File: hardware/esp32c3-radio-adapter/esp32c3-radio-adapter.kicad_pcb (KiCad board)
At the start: 2 copper layers, 29 x 36.5 mm, 10 parts, among them J1 Conn_01x08, J2 Conn_01x08, J3 E07-M1101D_or_Ra-02, J4 Expansion

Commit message: Adapters: GPIO map that lets the same socket take all three radio boards
The green D-Sun CC1101 board plugs into the socket adapter's 2x4 socket
too; only its signal order differs, which the firmware absorbs with a pin
map per board.  What the hardware must guarantee is that no socket
position that carries a radio OUTPUT on any of the boards is an ESP32-C3
boot strapping pin (GPIO2/8/9).  Only position 4 (blue CSN, green SCK,
Ra-02 NSS) is an input on every board, so it takes GPIO9; GPIO8 moves to
the spare header and positions 5 and 6 are fed from GPIO3 and GPIO4.

Socket positions 3..8 are now GPIO10, 9, 3, 4, 7, 6.  Per-board maps:
blue E07 MOSI 4 SCK 3 CSN 9 MISO 7 GDO0 10 GDO2 6; green D-Sun MOSI 10
SCK 9 CSN 6 MISO 3 GDO0 7 GDO2 4; Ra-02 MOSI 4 SCK 3 NSS 9 MISO 7 RST 10
DIO0 6.  The README also describes telling the two CC1101 boards apart
passively at power-up (an unconfigured CC1101 clocks XOSC/192 out of
GDO0, on GPIO10 for the blue board and GPIO7 for the green).

Socket adapter routing, still entirely on the back copper: GPIO9 leaves
its pad sideways into the gap before GPIO10 and drops into position 4;
MISO takes the column under GPIO8's pad; SCK and MOSI come down from the
power row through the gaps either side of GPIO8's pad, and GPIO8 climbs
between them to the header (now 3V3, 8, 2, 1, 0, 21TX, 20RX).

SX1278 module adapter: same GPIOs with MOSI and SCK swapped (GPIO3/4) so
its bottom copper nests, NSS on GPIO9 via the top-copper bus, RESET on
GPIO8 (an ESP32 output).

Jumper-wire diagrams: one layout serves all three boards; GPIO4 and GPIO3
take the ribbon's white and black; the Ra-02 strap goes to GPIO1 (GPIO4
is now MOSI).  Both adapters pass ERC and DRC.

Co-Authored-By: Claude Fable 5.1 <noreply@anthropic.com>
Claude-Session: https://claude.ai/code/session_01JoGdh4Cg3VtTTDZi4gQuiN
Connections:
- J1 pad 4: MOSI -> GPIO8
- J1 pad 5: SCK -> CSN_NSS
- J2 pad 4: GPIO4 -> MOSI
- J2 pad 5: GPIO3 -> SCK
- J2 pad 8: CSN_NSS -> GPIO0
- J4 pad 2: GPIO4 -> GPIO8
- J4 pad 3: GPIO3 -> GPIO2
- J4 pad 4: GPIO2 -> GPIO1
- J4 pad 5: GPIO1 -> GPIO0
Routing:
- net GPIO8: track 0.00 -> 21.7 mm
- net CSN_NSS: track 32.2 -> 11.8 mm
- net SCK: track 6.76 -> 24.5 mm
- net MOSI: track 11.8 -> 29.6 mm
- net GPIO0: track 0.00 -> 6.43 mm
- net GPIO4: track 5.01 -> 0.00 mm
- net GPIO3: track 5.01 -> 0.00 mm
- net GPIO2: track 5.01 -> 6.43 mm
- net GPIO1: track 5.01 -> 6.43 mm
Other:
- board text added: "E07-M1101D / D-Sun / Ra-02"
- board text removed: "E07-M1101D (Ra-02 breakout)"

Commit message: Socket adapter: move CSN/NSS off the GPIO9 boot strap to GPIO1
On the bench (2026-09-06) the CC1101/Ra-02 nodes powered straight into USB
download mode every reset and never ran the firmware.  Root cause: socket
position 4 (CSN on the blue board, SCK on the green, NSS on the Ra-02) was
GPIO9, the ESP32-C3 BOOT strap.  A radio pin loads that net with enough
capacitance that, through the chip's weak internal pull-up, it rises too
slowly for the mask ROM to read it high at reset, so the ROM latches BOOT low
and enters download mode.  It is not the firmware -- the ROM samples the strap
before any code runs -- and it is not fixable in software.

Fix, single layer as before: position 4 now takes GPIO1 (routed from the power
row, across between the SuperMini rows and into the pad from the left).  GPIO9
is left unconnected -- an unconnected strap floats high on the internal
pull-up, the safest state -- so the socket now carries no strap at all.  The
expansion header keeps its proven 7-pin geometry: GPIO1's old slot becomes a
second 3V3, and GPIO8/GPIO2 (the straps that stay exposed there) each get an
optional do-not-populate pull-up-to-3V3 footprint (R2/R3) bridging to the
adjacent 3V3 pin.  ERC/DRC clean.

Firmware pin map changes by one pin only: CSN/SCK/NSS 9 -> 1; everything else
unchanged.

Co-Authored-By: Claude Opus 4.8 <noreply@anthropic.com>
Claude-Session: https://claude.ai/code/session_01JoGdh4Cg3VtTTDZi4gQuiN
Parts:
- added R2: 4k7, Adapter:R_0805_HeaderPullup, F.Cu at (108.2, 102.5)
- added R3: 4k7, Adapter:R_0805_HeaderPullup, F.Cu at (113.2, 102.5)
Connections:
- J1 pad 5: CSN_NSS -> GPIO9
- J2 pad 7: GPIO1 -> CSN_NSS
- J4 pad 4: GPIO1 -> +3V3
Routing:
- net CSN_NSS: track 11.8 -> 29.6 mm
- net GPIO1: track 6.43 -> 0.00 mm
- net +3V3: track 64.0 -> 65.4 mm
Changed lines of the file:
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@@
 	(net 3 "MISO")
 	(net 4 "GPIO8")
-	(net 5 "CSN_NSS")
+	(net 5 "GPIO9")
 	(net 6 "GDO0_RST")
 	(net 7 "GPIO20")
@@
 	(net 13 "SCK")
 	(net 14 "GPIO2")
-	(net 15 "GPIO1")
+	(net 15 "CSN_NSS")
 	(net 16 "GPIO0")
 	(footprint "Adapter:SuperMini_Row_1x08_P2.54mm_THT_Castellated_Down"
@@
 			(layers "*.Cu" "*.Mask")
 			(remove_unused_layers no)
-			(net 5 "CSN_NSS")
+			(net 5 "GPIO9")
 			(pinfunction "Pin_5")
 			(pintype "passive")
@@
 			(layers "*.Cu" "*.Mask")
 			(remove_unused_layers no)
-			(net 15 "GPIO1")
+			(net 15 "CSN_NSS")
 			(pinfunction "Pin_7")
 			(pintype "passive")
@@
 			(layers "*.Cu" "*.Mask")
 			(remove_unused_layers no)
-			(net 5 "CSN_NSS")
+			(net 15 "CSN_NSS")
 			(pinfunction "Pin_4")
 			(pintype "passive")
@@
 			(layers "*.Cu" "*.Mask")
 			(remove_unused_layers no)
-			(net 15 "GPIO1")
+			(net 11 "+3V3")
 			(pinfunction "Pin_4")
 			(pintype "passive")
@@
 		)
 	)
+	(footprint "Adapter:R_0805_HeaderPullup"
+		(layer "F.Cu")
+		(at 108.15 102.55)
+		(descr "0805 resistor bridging two adjacent 2.54 mm header pins, on the back copper (optional strap pull-up)")
+		(tags "resistor 0805 pull-up header")
+		(sheetname "/")
+		(sheetfile "esp32c3-radio-adapter.kicad_sch")
+		(property "Reference" "R2"
+			(at 0 -1.8 0)
+			(layer "F.SilkS")
+			(hide yes)
+			(effects
+				(font
+					(size 0.8 0.8)
+					(thickness 0.12)
+				)
+			)
+		)
+		(property "Value" "4k7"
+			(at 0 1.8 0)
+			(layer "F.Fab")
+			(hide yes)
+			(effects
+				(font
+					(size 0.8 0.8)
+					(thickness 0.12)
+				)
+			)
+		)
+		(property "Datasheet" ""
+			(at 0 0 0)
+			(layer "F.Fab")
+			(hide yes)
+			(effects
+				(font
+					(size 1.27 1.27)
+					(thickness 0.1905)
+				)
+			)
+		)
+		(property "Description" ""
+			(at 0 0 0)
+			(layer "F.Fab")
+			(hide yes)
+			(effects
+				(font
+					(size 1.27 1.27)
+					(thickness 0.1905)
+				)
+			)
+		)
+		(attr smd)
+		(fp_text user "${REFERENCE}"
+			(at 0 -1.8 0)
+			(layer "F.Fab")
+			(effects
+				(font
+					(size 0.6 0.6)
+					(thickness 0.09)
+				)
+			)
+		)
+		(fp_rect
+			(start -0.65 -1)
+			(end 0.65 1)
+			(stroke
+				(width 0.1)
+				(type solid)
+			)
+			(fill no)
+			(layer "B.Fab")
+		)
+		(pad "1" smd rect
+			(at -1.27 0)
+			(size 1.4 1.2)
+			(layers "B.Cu" "B.Mask" "B.Paste")
+			(net 11 "+3V3")
+			(pinfunction "Pin_1")
+			(pintype "passive")
+		)
+		(pad "2" smd rect
+			(at 1.27 0)
+			(size 1.4 1.2)
+			(layers "B.Cu" "B.Mask" "B.Paste")
+			(net 4 "GPIO8")
+			(pinfunction "Pin_2")
+			(pintype "passive")
+		)
+		(embedded_fonts no)
+	)
+	(footprint "Adapter:R_0805_HeaderPullup"
+		(layer "F.Cu")
+		(at 113.23 102.55)
+		(descr "0805 resistor bridging two adjacent 2.54 mm header pins, on the back copper (optional strap pull-up)")
+		(tags "resistor 0805 pull-up header")
+		(sheetname "/")
+		(sheetfile "esp32c3-radio-adapter.kicad_sch")
+		(property "Reference" "R3"
+			(at 0 -1.8 0)
+			(layer "F.SilkS")
+			(hide yes)
+			(effects
+				(font
+					(size 0.8 0.8)
+					(thickness 0.12)
+				)
+			)
+		)
+		(property "Value" "4k7"
+			(at 0 1.8 0)
+			(layer "F.Fab")
+			(hide yes)
+			(effects
+				(font
+					(size 0.8 0.8)
+					(thickness 0.12)
+				)
+			)
+		)
+		(property "Datasheet" ""
+			(at 0 0 0)
+			(layer "F.Fab")
+			(hide yes)
+			(effects
+				(font
+					(size 1.27 1.27)
+					(thickness 0.1905)
+				)
+			)
+		)
+		(property "Description" ""
+			(at 0 0 0)
+			(layer "F.Fab")
+			(hide yes)
+			(effects
+				(font
+					(size 1.27 1.27)
+					(thickness 0.1905)
+				)
+			)
+		)
+		(attr smd)
+		(fp_text user "${REFERENCE}"
+			(at 0 -1.8 0)
+			(layer "F.Fab")
+			(effects
+				(font
+					(size 0.6 0.6)
+					(thickness 0.09)
+				)
+			)
+		)
+		(fp_rect
+			(start -0.65 -1)
+			(end 0.65 1)
+			(stroke
+				(width 0.1)
+				(type solid)
+			)
+			(fill no)
+			(layer "B.Fab")
+		)
+		(pad "1" smd rect
+			(at -1.27 0)
+			(size 1.4 1.2)
+			(layers "B.Cu" "B.Mask" "B.Paste")
+			(net 14 "GPIO2")
+			(pinfunction "Pin_1")
+			(pintype "passive")
+		)
+		(pad "2" smd rect
+			(at 1.27 0)
+			(size 1.4 1.2)
+			(layers "B.Cu" "B.Mask" "B.Paste")
+			(net 11 "+3V3")
+			(pinfunction "Pin_2")
+			(pintype "passive")
+		)
+		(embedded_fonts no)
+	)
 	(footprint "Adapter:MountingHole_2.2mm_M2"
 		(layer "F.Cu")
@@
 		)
 	)
-	(gr_text "CSN/NSS"
-		(at 111.4 118.94 90)
-		(layer "F.SilkS")
-		(effects
-			(font
-				(size 0.5 0.5)
-				(thickness 0.075)
-			)
-		)
-	)
-	(gr_text "CSN/NSS"
-		(at 111.4 118.94 270)
-		(layer "B.SilkS")
-		(effects
-			(font
-				(size 0.5 0.5)
-				(thickness 0.075)
-			)
-			(justify mirror)
-		)
-	)
 	(gr_text "2"
 		(at 113.94 103.9 0)
@@
 	(gr_text "20"
 		(at 116.48 125.34 0)
+		(layer "B.SilkS")
+		(effects
+			(font
+				(size 0.5 0.5)
+				(thickness 0.075)
+			)
+			(justify mirror)
+		)
+	)
+	(gr_text "CSN/NSS"
+		(at 116.48 110.3 90)
+		(layer "F.SilkS")
+		(effects
+			(font
+				(size 0.5 0.5)
+				(thickness 0.075)
+			)
+		)
+	)
+	(gr_text "CSN/NSS"
+		(at 116.48 110.3 270)
 		(layer "B.SilkS")
 		(effects
@@
 		)
 	)
-	(gr_text "1"
+	(gr_text "3V3"
 		(at 114.5 101.25 0)
 		(layer "F.SilkS")
@@
 		)
 	)
-	(gr_text "1"
+	(gr_text "3V3"
 		(at 114.5 101.25 0)
 		(layer "B.SilkS")
@@
 	)
 	(segment
-		(start 111.4 122.24)
-		(end 112.67 122.24)
-		(width 0.25)
-		(layer "B.Cu")
-		(net 5)
-	)
-	(segment
-		(start 112.67 122.24)
+		(start 116.48 107)
+		(end 116.48 112)
+		(width 0.25)
+		(layer "B.Cu")
+		(net 15)
+	)
+	(segment
+		(start 116.48 112)
+		(end 112.67 112)
+		(width 0.25)
+		(layer "B.Cu")
+		(net 15)
+	)
+	(segment
+		(start 112.67 112)
 		(end 112.67 131.54)
 		(width 0.25)
 		(layer "B.Cu")
-		(net 5)
+		(net 15)
 	)
 	(segment
@@
 		(width 0.25)
 		(layer "B.Cu")
-		(net 5)
+		(net 15)
 	)
 	(segment
@@
 	)
 	(segment
+		(start 114.5 101.2)
+		(end 114.5 102.55)
+		(width 0.25)
+		(layer "B.Cu")
+		(net 11)
+	)
+	(segment
 		(start 113.94 107)
 		(end 113.94 104)
@@
 	)
 	(segment
-		(start 116.48 107)
-		(end 116.48 104)
-		(width 0.25)
-		(layer "B.Cu")
-		(net 15)
-	)
-	(segment
-		(start 116.48 104)
-		(end 114.5 104)
-		(width 0.25)
-		(layer "B.Cu")
-		(net 15)
-	)
-	(segment
-		(start 114.5 104)
-		(end 114.5 102.55)
-		(width 0.25)
-		(layer "B.Cu")
-		(net 15)
-	)
-	(segment

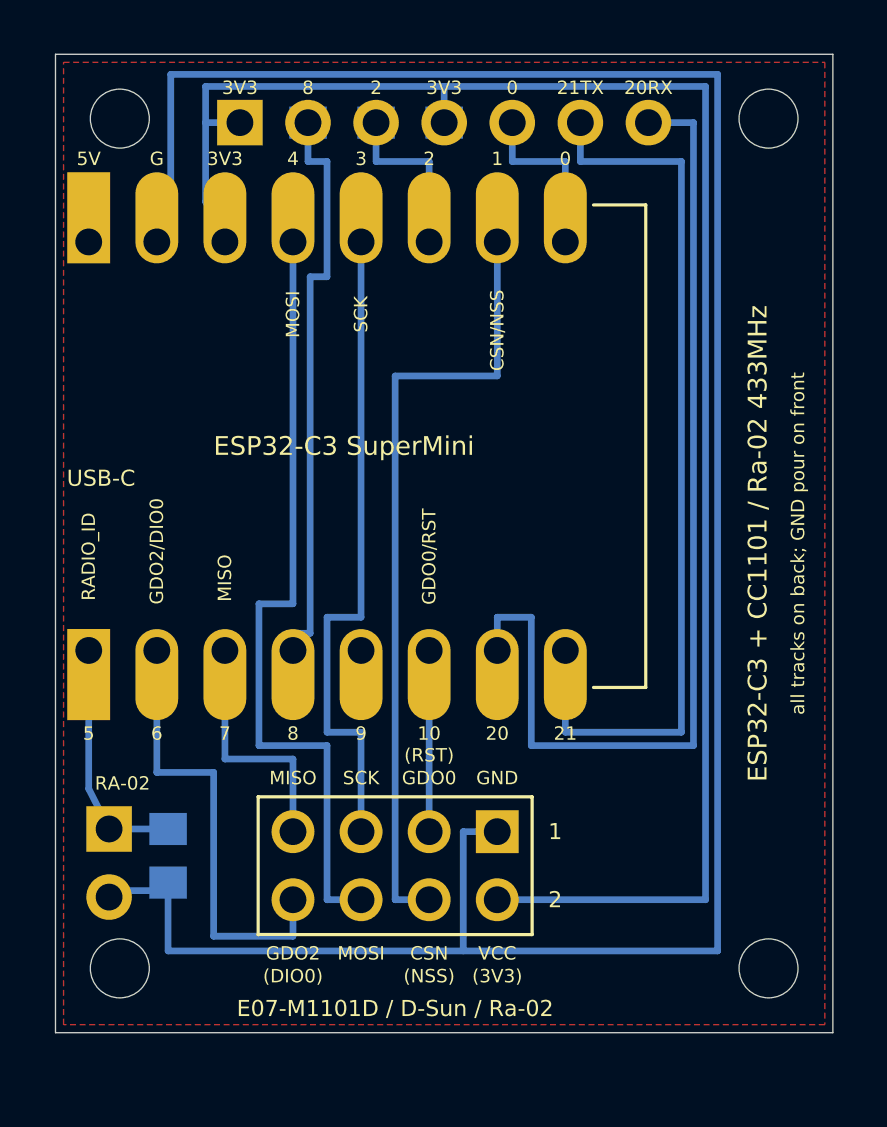
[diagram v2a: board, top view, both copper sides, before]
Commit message: Socket adapter: J5, a fly-wire header for the SX1278's DIO2/DATA pin
In the SX1278's continuous mode the raw bitstream reaches the outside
world only on DIO2/DATA -- the FIFO and packet handler are inactive, and
Table 29 gives no other DIO that can carry it in Rx.  Packet mode can't
stand in: it only carries what the chip's packet handler can frame, which
is fine for the Fineoffset stations but useless for the OOK remotes this
node exists to hear and key.  DIO2 is the SX1278's GDO2, and the Ra-02
breakout leaves it on the module edge, unconnected.

Add J5, a 1x2 header carrying GPIO21 and GPIO20, so one wire from an
Ra-02's DIO2 pad reaches a GPIO.  GPIO20 is that pin; both stay on J4 as
well, so nothing is lost -- one net, brought out twice.

Placing it took the board from 36.5 to 38.0 mm tall.  A 2.54 mm header
body and both plugged-in boards all sit at board level, so the header has
to be clear of them in plan view, and the only such region is the band
between the SuperMini's body and the radio board's top edge.  At 36.5 mm
that band is 4.08 mm, which leaves 0.79 mm either side of the body;
1.5 mm more opens it to 5.58 mm and takes both margins to 1.54 mm.

Routing stays single-sided.  GPIO21 drops right of GPIO20, so it must
take the lane above J5's pads (25.29) and stubs down into pin 1; GPIO20
takes the lane below (27.8) and climbs the strip straight through its own
pad, pin 2.  That fixes which net is on which pin: GPIO20's strip lane
has to pass through a pad of its own net, and the gap right of pin 2 is
only 0.235 mm.  The four strip lanes shift left 0.45 mm to make room
(GPIO21 22.9, GPIO20 23.35) and 3V3/GND move out to 24.55/25.0, still
0.375 mm clear of the M2 holes.

GND is not on J5: reaching it would mean crossing the 3V3 strip lane, and
it isn't needed -- the boards already share GND through the socket.

The SX1278 module adapter is untouched; its pin allocation is to be
brought into line with this board separately.

Co-Authored-By: Claude Opus 5 (1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
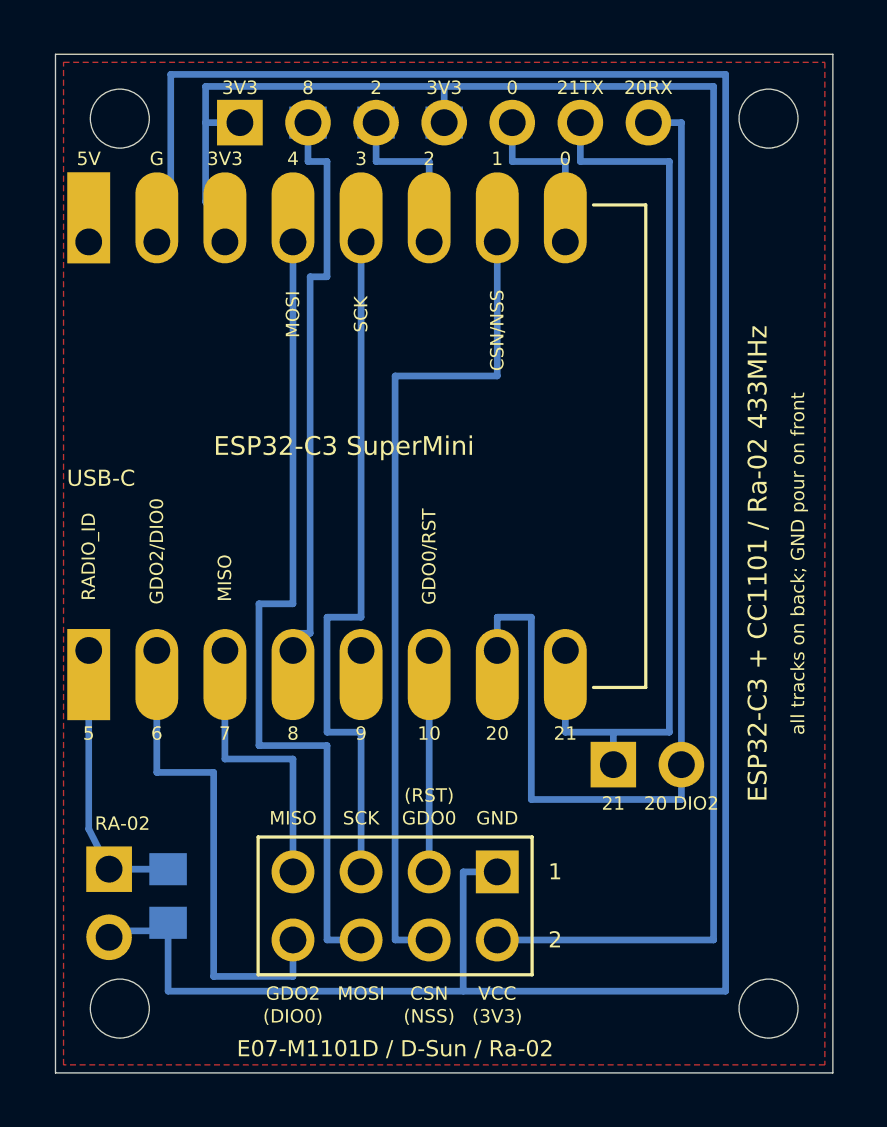
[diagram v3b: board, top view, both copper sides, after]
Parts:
- added J5: DIO2/DATA, Adapter:PinHeader_1x02_P2.54mm_Vertical, F.Cu at (120.8, 126.5)
- moved H3 1.50 mm to (102.4, 135.6)
- moved H4 1.50 mm to (126.6, 135.6)
- moved J3 1.50 mm to (116.5, 130.5)
- moved JP1 1.50 mm to (102.0, 130.4)
- moved R1 1.50 mm to (104.2, 131.4)
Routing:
- net GPIO20: track 38.3 -> 41.4 mm
- net GND: track 90.4 -> 92.5 mm
- net +3V3: track 65.4 -> 67.5 mm
- net SCK: track 24.5 -> 26.0 mm
- net RADIO_ID: track 9.04 -> 10.5 mm
- net MOSI: track 29.6 -> 31.1 mm
- net MISO: track 9.30 -> 10.8 mm
- net GDO2_DIO0: track 17.1 -> 18.6 mm
- net GDO0_RST: track 6.76 -> 8.26 mm
- net CSN_NSS: track 29.6 -> 31.1 mm
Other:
- board size 29 x 36.5 mm -> 29 x 38 mm
- board text added: "20 DIO2"
